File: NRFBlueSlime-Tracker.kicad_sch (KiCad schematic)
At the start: 41 parts, among them J1 USB_C_Receptacle_USB2.0_16P, J2 Conn_01x05, J3 Conn_01x02_MountingPin, Q1 AO3401A, SW1 TS-1088-AR02016, U1 ANNA-B402-00B, U2 ICM-42688-P, U3 LIS2MDL, U4 ME6211C33R5G, U5 TP4057, X1 S2D32.768KB20F30T

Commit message: dhshdfsdgjfhfghj
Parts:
- J3: value Conn_01x02_MountingPin -> 532610271
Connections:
- no-connect marks 8 -> 7
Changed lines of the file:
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@@
 	)
 	(no_connect
-		(at 27.94 26.67)
-	)
-	(no_connect
 		(at 27.94 80.01)
 	)
@@
 			)
 		)
-		(property "Value" "Conn_01x02_MountingPin"
+		(property "Value" "532610271"
 			(at 139.7 110.8455 0)
 			(effects

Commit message: nrf52832 rev
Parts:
- removed C8, C9: 10u, Capacitor_SMD:C_0402_1005Metric, symbol Device:C
- removed D1: 1N5819WS, Diode_SMD:D_SOD-323, symbol Diode:1N5819WS
- removed D2: PRTR5V0U2X, Package_TO_SOT_SMD:SOT-143, symbol Power_Protection:PRTR5V0U2X
- removed J1: USB_C_Receptacle_USB2.0_16P, Connector_USB:USB_C_Receptacle_G-Switch_GT-USB-7010ASV, symbol Connector:USB_C_Receptacle_USB2.0_16P
- removed J2: Conn_01x05, Connector_PinHeader_2.54mm:PinHeader_1x05_P2.54mm_Vertical, symbol Connector_Generic:Conn_01x05
- removed LED1: NCD0402R1, LED_SMD:LED_0402_1005Metric, symbol Device:LED
- removed LED2: NCD0402G1, LED_SMD:LED_0402_1005Metric, symbol Device:LED
- removed Q1: AO3401A, Package_TO_SOT_SMD:SOT-23, symbol Transistor_FET:AO3401A
- removed R1, R2: 5.1k, Resistor_SMD:R_0402_1005Metric, symbol Device:R
- removed R6: 2.2k, Resistor_SMD:R_0402_1005Metric, symbol Device:R
- removed R7: 4.7k, Resistor_SMD:R_0402_1005Metric, symbol Device:R
- removed R9: 10k, Resistor_SMD:R_0402_1005Metric, symbol Device:R
- removed U1: ANNA-B402-00B, b402:ANNA-B402_UBL, symbol b402:ANNA-B402-00B
- removed U5: TP4057, nrfslime:SOT-23-6_L2.9-W1.6-P0.95-LS2.8-BL, symbol nrfslime:TP4057
- added J2: Conn_01x06_Pin, Connector_PinHeader_2.54mm:PinHeader_1x06_P2.54mm_Vertical, symbol Connector:Conn_01x06_Pin
- added R4: 1M, Resistor_SMD:R_0402_1005Metric, symbol Device:R
- added U1: ISP1507-AX-ST, ISP1507AXST, symbol ISP1507-AX-ST:ISP1507-AX-ST
- added U5: SRV05-4, Package_TO_SOT_SMD:SOT-23-6, symbol Power_Protection:SRV05-4
- R2: renamed from R8; value 220 -> 470
- renumbered C3 to C1, C2 to C10, C13 to C11, C4 to C2, C6 to C3, C7 to C4, C11 to C6, C12 to C7, C10 to C8, C1 to C9, J3 to J1, LED3 to LED1, R12 to R1, R10 to R3, R3 to R5, R4 to R6, R5 to R7, R11 to R8
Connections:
- net VDC is gone; now on net +BATT: C6.1, U4.1 (VIN), U4.3 (CE)
- net +3V3: now also R4.1, U1.26 (VCC)
- net +BATT: now also J2.1 (Pin_1), U5.5 (VP)
- net BATLVL: now also U1.38 (P0_03/AIN1)
- net GND: now also J2.5 (Pin_5), U1.1 (VSS_1), U1.10 (VSS_4), U1.12 (VSS_5), U1.14 (VSS_6), U1.16 (VSS_7), U1.18 (VSS_8), U1.21 (VSS_9), U1.23 (VSS_10), U1.24 (VSS_11), U1.25 (VSS_12), U1.31 (VSS_13), U1.7 (VSS_2), U1.8 (VSS_3), U5.2 (VN); no longer R8.2
- net INT: now also U1.43 (P0_11)
- net LED: now also U1.41 (P0_25)
- net RST: now also J2.4 (Pin_4), U1.13 (P0_21/NRESET), U5.4 (IO3)
- net SCL: now also U1.47 (P0_23)
- net SDA: now also U1.45 (P0_19)
- net SWC: now also J2.3 (Pin_3), U1.30 (SWDCLK), U5.3 (IO2)
- net SWD: now also J2.2 (Pin_2), U1.28 (SWDIO), U5.1 (IO1)
- new net: U1.20 (OUT_ANT), U1.22 (OUT_MOD)
- new net ADC_EN: R8.2, U1.40 (P0_02/AIN0)
- new net DOCK: J2.6 (Pin_6), R4.2, U1.32 (P0_08), U5.6 (IO4)
- no-connect marks 7 -> 15
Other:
- moved on the sheet: C10, C9

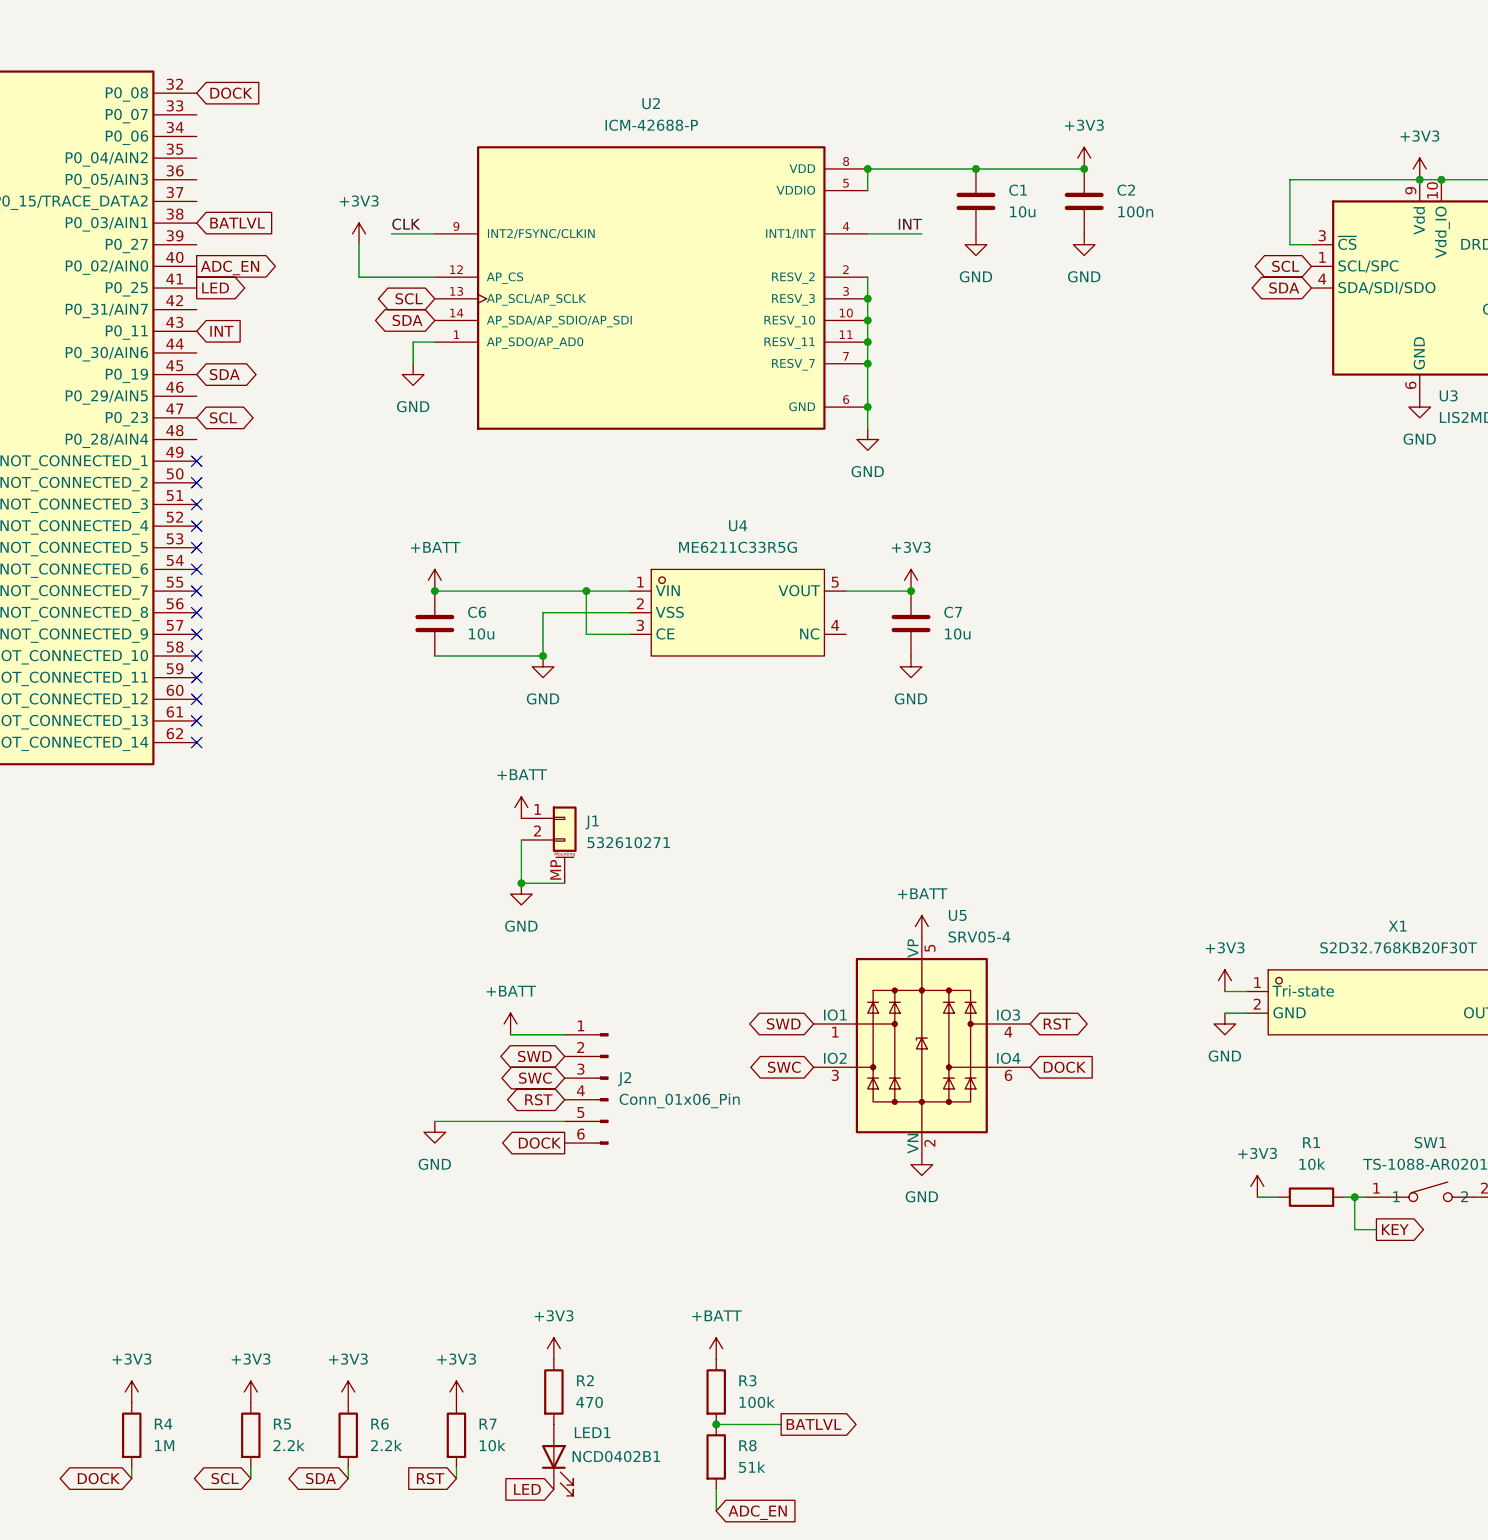
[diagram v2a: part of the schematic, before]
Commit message: use metric spacing for dock, route switch
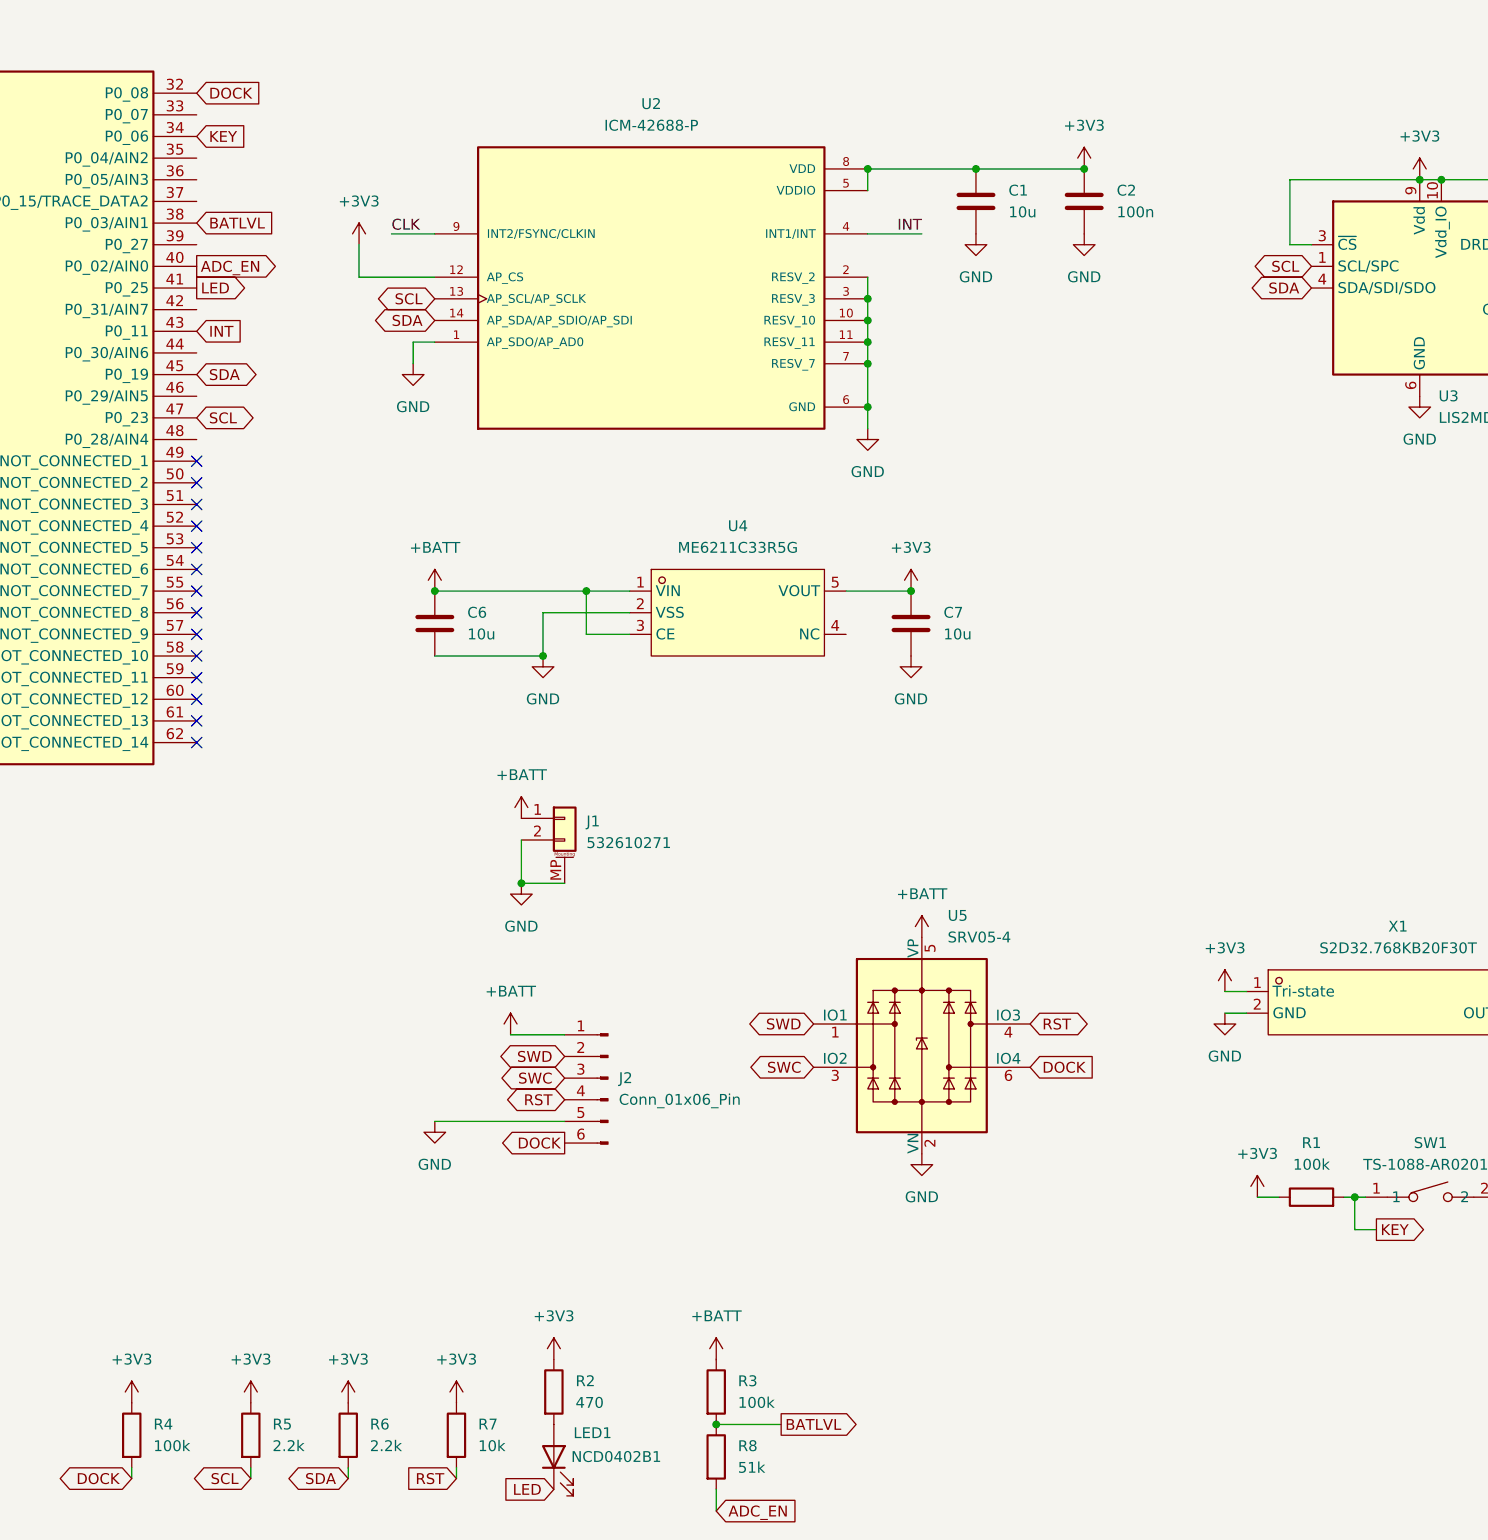
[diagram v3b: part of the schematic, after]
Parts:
- R1: value 10k -> 100k
- R4: value 1M -> 100k
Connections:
- net KEY: now also U1.34 (P0_06)
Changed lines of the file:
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@@
 		)
 	)
+	(global_label "KEY"
+		(shape input)
+		(at 93.98 27.94 0)
+		(fields_autoplaced yes)
+		(effects
+			(font
+				(size 1.27 1.27)
+			)
+			(justify left)
+		)
+		(property "Intersheetrefs" "${INTERSHEET_REFS}"
+			(at 100.4728 27.94 0)
+			(effects
+				(font
+					(size 1.27 1.27)
+				)
+				(justify left)
+				(hide yes)
+			)
+		)
+	)
 	(global_label "SWC"
 		(shape bidirectional)
@@
 			)
 		)
-		(property "Value" "10k"
+		(property "Value" "100k"
 			(at 224.79 148.59 90)
 			(effects
@@
 			)
 		)
-		(property "Value" "1M"
+		(property "Value" "100k"
 			(at 88.9 181.6099 0)
 			(effects

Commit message: done nrf52840 ver
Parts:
- removed C10: 100n, Capacitor_SMD:C_0402_1005Metric, symbol Device:C
- removed C9: 1u, Capacitor_SMD:C_0402_1005Metric, symbol Device:C
- removed J2: Conn_01x06_Pin, Connector_PinHeader_2.54mm:PinHeader_1x06_P2.54mm_Vertical, symbol Connector:Conn_01x06_Pin
- removed R7: 10k, Resistor_SMD:R_0402_1005Metric, symbol Device:R
- removed U1: ISP1507-AX-ST, ISP1507AXST, symbol ISP1507-AX-ST:ISP1507-AX-ST
- removed U5: SRV05-4, Package_TO_SOT_SMD:SOT-23-6, symbol Power_Protection:SRV05-4
- added C12: 1u, Capacitor_SMD:C_0402_1005Metric, symbol Device:C
- added C13: 100n, Capacitor_SMD:C_0402_1005Metric, symbol Device:C
- added C15: 1u, Capacitor_SMD:C_0603_1608Metric, symbol Device:C
- added C16: 10u, Capacitor_SMD:C_0603_1608Metric, symbol Device:C
- added D1: 1N5819WS, Diode_SMD:D_SOD-323, symbol Diode:1N5819WS
- added J3: USB_C_Receptacle_USB2.0_16P, Connector_USB:USB_C_Receptacle_G-Switch_GT-USB-7010ASV, symbol Connector:USB_C_Receptacle_USB2.0_16P
- added LED2: NCD0402R1, LED_SMD:LED_0402_1005Metric, symbol Device:LED
- added LED3: NCD0402G1, LED_SMD:LED_0402_1005Metric, symbol Device:LED
- added Q1: AO3401A, Package_TO_SOT_SMD:SOT-23, symbol Transistor_FET:AO3401A
- added R10, R9: 5.1k, Resistor_SMD:R_0402_1005Metric, symbol Device:R
- added R11: 2.2k, Resistor_SMD:R_0402_1005Metric, symbol Device:R
- added R12: 10k, Resistor_SMD:R_0402_1005Metric, symbol Device:R
- added R13: 1.6k, Resistor_SMD:R_0402_1005Metric, symbol Device:R
- added R14, R15: 27, Resistor_SMD:R_0402_1005Metric, symbol Device:R
- added SW2: SK-3296S-01-L1, switch:SW-SMD_3P-P1.50_L2.7-W6.6, symbol switch:SK-3296S-01-L1
- added TP1, TP2, TP3, TP4, TP5: TestPoint, TestPoint:TestPoint_Pad_1.0x1.0mm, symbol Connector:TestPoint
- added TV1: PRTR5V0U2X, Package_TO_SOT_SMD:SOT-143, symbol Power_Protection:PRTR5V0U2X
- added U1: MDBT50Q-1MV2, RF_Module:Raytac_MDBT50Q, symbol RF_Module:MDBT50Q-1MV2
- added U5: TP4057-42-SOT26-R, Package_TO_SOT_SMD:SOT-23-6, symbol Battery_Management:TP4057
- C1, C3, C6, C7: footprint Capacitor_SMD:C_0402_1005Metric -> Capacitor_SMD:C_0603_1608Metric
- C8: value 10u -> 100n
- R4: value 100k -> 1k
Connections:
- net +3V3: now also TP1.1, U1.28 (VDD), U1.30 (VDDH); no longer R4.1
- net +BATT: now also C16.1, Q1.3 (D), U5.3 (BAT); no longer C6.1, U4.1 (VIN), U4.3 (CE)
- net ADC_EN: now also U1.11 (P0.02)
- net BATLVL: now also U1.9 (P0.03)
- net GND: now also C12.2, C13.2, C15.2, C16.2, J3.A1 (GND), J3.A12 (GND), J3.B1 (GND), J3.B12 (GND), J3.S1 (SHIELD), R10.2, R11.2, R12.2, R13.1, R9.2, TP5.1, TV1.1 (GND), U1.1 (GND), U1.15 (GND), U1.2 (GND), U1.33 (GND), U1.55 (GND), U5.2 (GND)
- net INT: now also U1.27 (P0.11)
- net KEY: now also U1.22 (P0.06)
- net LED: now also U1.49 (P0.25)
- net SCL: now also U1.45 (P0.23)
- net SDA: now also U1.42 (P0.19)
- net SWC: now also TP3.1, U1.53 (SWDCLK)
- net SWD: now also TP2.1, U1.51 (SWDIO)
- net DOCK renamed VBUS
- net VBUS: now also C12.1, C13.1, C15.1, D1.2 (A), J3.A4 (VBUS), J3.A9 (VBUS), J3.B4 (VBUS), J3.B9 (VBUS), Q1.1 (G), R12.1, TV1.4 (VCC), U1.32 (VBUS), U5.4 (V_{CC})
- new net: LED2.1 (K), U5.1 (~{CHRG})
- new net: LED2.2 (A), LED3.2 (A), R4.1
- new net: J3.B5 (CC2), R10.1
- new net: LED3.1 (K), U5.5 (STDBY)
- new net: R13.2, U5.6 (PROG)
- new net: J3.A5 (CC1), R9.1
- new net: R15.2, U1.35 (D+)
- new net: R14.2, U1.34 (D-)
- new net DN: J3.A7 (D-), J3.B7 (D-), R14.1, TV1.2 (I/O1)
- new net DP: J3.A6 (D+), J3.B6 (D+), R15.1, TV1.3 (I/O2)
- new net EN: R11.1, SW2.2, U4.3 (CE)
- new net NRST: TP4.1, U1.43 (P0.21)
- new net VDC: C6.1, D1.1 (K), Q1.2 (S), SW2.3, U4.1 (VIN)
- no-connect marks 15 -> 6
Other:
- moved on the sheet: C11, C8, J1, LED1, R1, R2, R3, R5, R6, R8, SW1, X1

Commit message: new ver
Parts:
- removed R1: 100k, Resistor_SMD:R_0402_1005Metric, symbol Device:R
- removed U1: MDBT50Q-1MV2, RF_Module:Raytac_MDBT50Q, symbol RF_Module:MDBT50Q-1MV2
- removed U4: ME6211C33R5G, nrfslime:SOT-353_L2.1-W1.3-P0.65-LS2.3-BL, symbol nrfslime:ME6211C33R5G
- added C10: 100n, Capacitor_SMD:C_0402_1005Metric, symbol Device:C
- added C9: 1u, Capacitor_SMD:C_0402_1005Metric, symbol Device:C
- added TP6: TestPoint, TestPoint:TestPoint_Pad_1.0x1.0mm, symbol Connector:TestPoint
- added U1: ISP1807-LR-RS, ISP1807-LR-RS:ISP1807-LR-RS, symbol ISP1807-LR-RS:ISP1807-LR-RS
- added U4: ME6211C33U4AG-N, nrfslime:FBP4L_L1.0-W1.0-P0.65-BL-EP, symbol nrfslime:ME6211C33U4AG-N
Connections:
- net +3V3: now also C10.1, C9.1, U1.26 (VCC_NRF), U4.1 (VOUT); no longer X1.1 (Tri-state)
- net ADC_EN: now also U1.60 (P1_10)
- net BATLVL: now also U1.38 (P0_03_AIN1)
- net GND: now also SW1.2, C10.2, C9.2, U1.1 (VSS), U1.14 (VSS), U1.16 (VSS), U1.18 (VSS), U1.21 (VSS), U1.23 (VSS), U1.24 (VSS), U1.25 (VSS), U1.31 (VSS), U1.7 (VSS), U4.2 (VSS)
- net INT: now also U1.32 (P0_08)
- net KEY: now also C11.1, U1.29 (P0_13)
- net LED: now also U1.33 (P0_07_TRACECLK)
- net NRST: now also U1.13 (P0_18_RESET)
- net SCL: now also U1.34 (P0_06)
- net SDA: now also U1.6 (P0_26)
- net SWC: now also U1.30 (SWDCLK)
- net SWD: now also U1.28 (SWDIO)
- net VBUS: now also U1.12 (VBUS)
- net VDC: now also U4.4 (VIN)
- net at R15.2: now also U1.8 (D+)
- net at R14.2: now also U1.10 (D-)
- new net DOCK: TP6.1, U1.56 (P1_09_TRACEDATA3)
- new net LDO_EN: U1.46 (P0_29_AIN5), U4.3 (CE)
- new net OSC_EN: U1.48 (P0_28_AIN4), X1.1 (Tri-state)
- no-connect marks 6 -> 5
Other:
- moved on the sheet: C1, C11, C15, C16, C2, C3, C4, C5, C6, C7, C8, D1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

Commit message: redo schematic
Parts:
- removed R11: 2.2k, Resistor_SMD:R_0402_1005Metric, symbol Device:R
- removed R2: 470, Resistor_SMD:R_0402_1005Metric, symbol Device:R
- removed R9: 5.1k, Resistor_SMD:R_0402_1005Metric, symbol Device:R
- removed SW2: SK-3296S-01-L1, switch:SW-SMD_3P-P1.50_L2.7-W6.6, symbol switch:SK-3296S-01-L1
- removed TV1: PRTR5V0U2X, Package_TO_SOT_SMD:SOT-143, symbol Power_Protection:PRTR5V0U2X
- removed U1: ISP1807-LR-RS, ISP1807-LR-RS:ISP1807-LR-RS, symbol ISP1807-LR-RS:ISP1807-LR-RS
- removed U4: ME6211C33U4AG-N, nrfslime:FBP4L_L1.0-W1.0-P0.65-BL-EP, symbol nrfslime:ME6211C33U4AG-N
- added C16, C17: 22p, Capacitor_SMD:C_0603_1608Metric, symbol Device:C
- added D1, D2, D3, D4, D5, D6, D7: PESD5V0X1UB, Diode_SMD:D_SOD-882, symbol Diode:PESD5V0L1UL
- added L1: 2.2u, nrfslime:IND-SMD_L3.0-W3.0, symbol Device:L
- added R1: 5.1k, Resistor_SMD:R_0603_1608Metric, symbol Device:R
- added R13, R14: 100k, Resistor_SMD:R_0603_1608Metric, symbol Device:R
- added R7: 499k, Resistor_SMD:R_0603_1608Metric, symbol Device:R
- added U2: E73-2G4M08S1C, nrf:WIRELM-SMD_E73-2G4M08S1C, symbol nrf:E73-2G4M08S1C
- added U4: EA8103T5R, Package_TO_SOT_SMD:SOT-23-5, symbol nrfslime:EA8103T5R
- added Y1: Q13FC13500004, Crystal:Crystal_SMD_3215-2Pin_3.2x1.5mm, symbol Device:Crystal
- C11: value 100n -> 220n
- J1: renamed from J3; value USB_C_Receptacle_USB2.0_16P -> GT-USB-7010ASV
- R12: renamed from R13; value 1.6k -> 10k
- R2: renamed from R10; footprint Resistor_SMD:R_0402_1005Metric -> Resistor_SMD:R_0603_1608Metric
- R3: renamed from R14; footprint Resistor_SMD:R_0402_1005Metric -> Resistor_SMD:R_0603_1608Metric
- R4: renamed from R15; footprint Resistor_SMD:R_0402_1005Metric -> Resistor_SMD:R_0603_1608Metric
- R5: value 2.2k -> 1k
- R6: value 2.2k -> 965k; footprint Resistor_SMD:R_0402_1005Metric -> Resistor_SMD:R_0603_1608Metric
- R8: renamed from R12; value 10k -> 100k
- U1: renamed from U2; value ICM-42688-P -> ICM-45686
- X1: symbol nrfslime:S2D32.768KB20F30T -> Oscillator:ASCO
- renumbered C6 to C12, C7 to C13, C15 to C14, C16 to C15, C8 to C3, C3 to C4, C4 to C5, C5 to C6, C12 to C7, C13 to C8, D1 to D8, J1 to J2, R3 to R10, R8 to R11, R4 to R9
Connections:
- net +3V3: now also R5.2, L1.2, R13.2, R14.2, U2.19 (VCC), U2.23 (VDH); no longer R5.1, TP1.1, U1.12 (AP_CS), U3.3 (~{CS})
- net ADC_EN: now also U2.3 (P0.03); no longer R11.2
- net BATLVL: now also U2.15 (AI3)
- net DN: now also D1.1 (K)
- net DOCK: now also D7.1 (K), U2.7 (AI0)
- net DP: now also D2.1 (K)
- net GND: now also C14.1, D1.2 (A), D2.2 (A), D3.2 (A), D4.2 (A), D5.2 (A), D6.2 (A), D7.2 (A), R1.2, R7.2, U2.21 (GND), U2.5 (GND), U4.2 (GND); no longer C14.2, U1.1 (AP_SDO/AP_AD0)
- net INT: now also U2.9 (AI7)
- net KEY: now also U2.33 (P0.13)
- net LED: now also U2.10 (AI6)
- net OSC_EN: now also U2.4 (AI4)
- net SWC: now also D5.1 (K), U2.39 (SWC)
- net SWD: now also D4.1 (K), U2.37 (SWD)
- net VBUS: now also C14.2, TP1.1, D3.1 (K), U2.27 (VBUS); no longer C14.1
- net VDC: now also U4.1 (EN), U4.4 (VIN)
- net at LED1.2 (A): now also R5.1
- net at J1.A5 (CC1): now also R1.1
- net at R4.2: now also U2.31 (D+)
- net at R3.2: now also U2.29 (D-)
- net MISO: now reaches U3.7 (DRDY)
- net MISO: now also U1.1 (AP_SDO/AP_AD0), U2.2 (P1.10)
- net NRST renamed ~{RST}
- net ~{RST}: now also D6.1 (K), U2.26 (RST)
- net SCL renamed SCLK
- net SCLK: now also U2.17 (P1.09); no longer R5.2
- net SDA renamed MOSI
- net MOSI: now also U2.1 (P1.11); no longer R6.2
- new net: C16.1, U2.11 (XL1)
- new net: C16.2, Y1.1
- new net: L1.1, U4.3 (SW)
- new net: C17.2, Y1.2
- new net: C17.1, U2.13 (XL2)
- new net: R6.2, R7.1, U4.5 (FB)
- new net ~{ADC_EN}: R11.2
- new net ~{CS}_IMU: R13.1, U1.12 (AP_CS), U2.6 (P1.13)
- new net ~{CS}_MAG: R14.1, U2.35 (P0.24), U3.3 (~{CS})
- no-connect marks 5 -> 3
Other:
- moved on the sheet: C1, C11, C12, C13, C14, C15, C2, C3, C4, C5, C6, D8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
